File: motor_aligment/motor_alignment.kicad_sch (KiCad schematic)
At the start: 27 parts, among them J1 PWR_24V_IN, J2 SENSOR_IN, J3 LCD_I2C, J4 UART_DOWNLOAD, J5 JTAG, SW1 BTN, U1 LM2596S-5, U2 ADS1115, U3 ESP32-WROOM-32

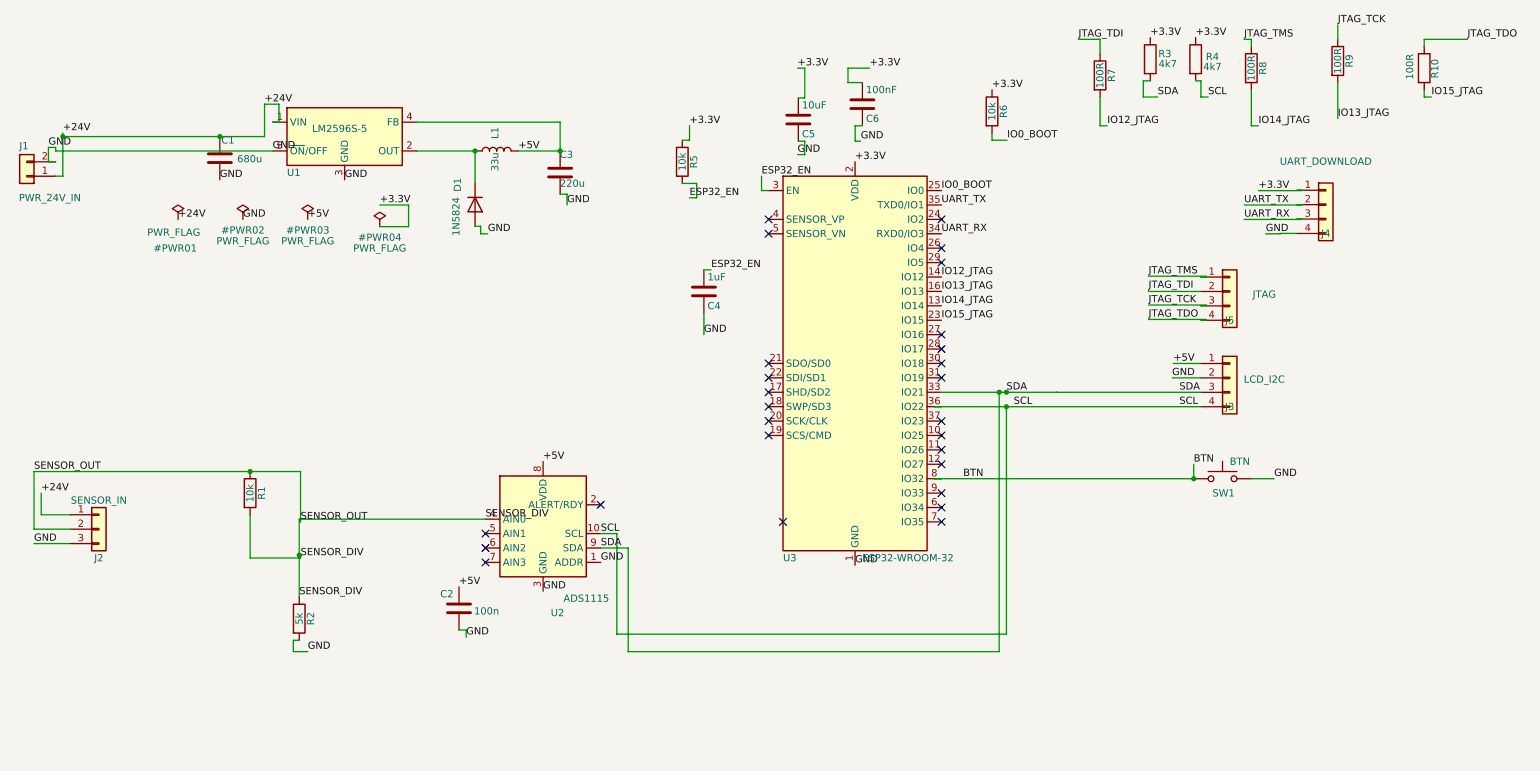
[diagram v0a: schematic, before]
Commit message: Add LCSC parameters and fix footprints for all components
- Added MPN, Manufacturer, JLCPCB_Type, Description, Datasheet properties
  to all 22 components from LCSC/JLCPCB database
- Fixed footprint mismatch: R7-R10 and C2/C6 corrected from 0402 to 0603
  to match purchased LCSC components
- ERC: 0 errors, 0 warnings

Co-Authored-By: Claude Sonnet 4.6 <noreply@anthropic.com>
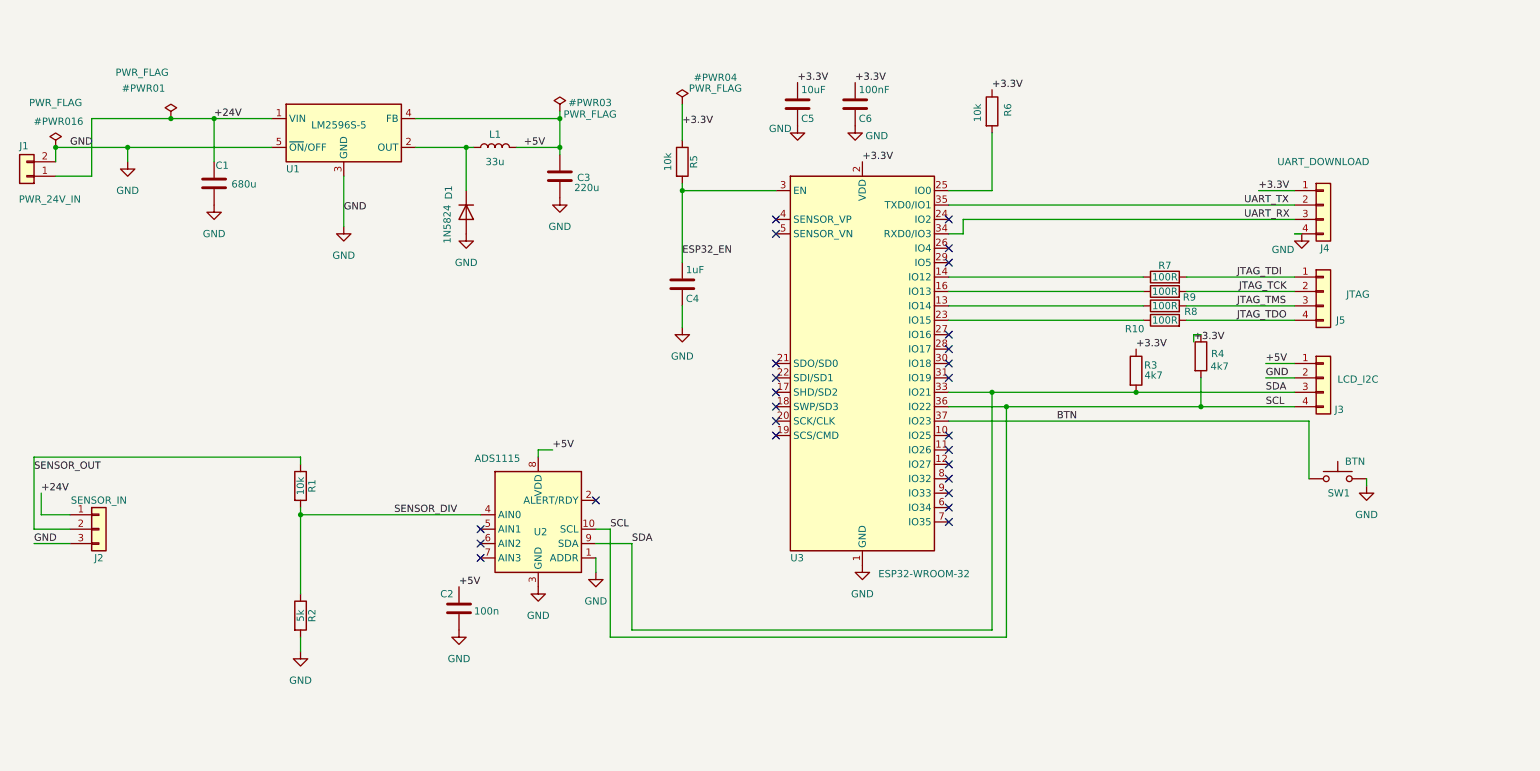
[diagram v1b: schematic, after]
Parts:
- C1: JLCPCB_Type (none) -> Extended; LCSC (none) -> C98216; MPN (none) -> RVT1V681M1213; Manufacturer (none) -> ROQANG
- C2, C6: footprint Capacitor_SMD:C_0402_1005Metric -> Capacitor_SMD:C_0603_1608Metric; JLCPCB_Type (none) -> Basic; LCSC (none) -> C14663; MPN (none) -> CC0603KRX7R9BB104; Manufacturer (none) -> YAGEO
- C3: JLCPCB_Type (none) -> Extended; LCSC (none) -> C3340; MPN (none) -> RVT1V221M0810; Manufacturer (none) -> Honor Elec
- C4: JLCPCB_Type (none) -> Basic; LCSC (none) -> C15849; MPN (none) -> CL10A105KB8NNNC; Manufacturer (none) -> Samsung Electro-Mechanics
- C5: JLCPCB_Type (none) -> Basic; LCSC (none) -> C15850; MPN (none) -> CL21A106KAYNNNE; Manufacturer (none) -> Samsung Electro-Mechanics
- D1: JLCPCB_Type (none) -> Basic; LCSC (none) -> C22452; MPN (none) -> SS54; Manufacturer (none) -> MDD（Microdiode Electronics）
- L1: JLCPCB_Type (none) -> Extended; LCSC (none) -> C840528; MPN (none) -> SRR1260-330M; Manufacturer (none) -> BOURNS
- R1, R5, R6: JLCPCB_Type (none) -> Basic; LCSC (none) -> C25804; MPN (none) -> 0603WAF1002T5E; Manufacturer (none) -> UNI-ROYAL(Uniroyal Elec)
- R10, R7, R8, R9: footprint Resistor_SMD:R_0402_1005Metric -> Resistor_SMD:R_0603_1608Metric; JLCPCB_Type (none) -> Basic; LCSC (none) -> C22775; MPN (none) -> 0603WAF1000T5E; Manufacturer (none) -> UNI-ROYAL(Uniroyal Elec)
- R2: JLCPCB_Type (none) -> Basic; LCSC (none) -> C23186; MPN (none) -> 0603WAF5101T5E; Manufacturer (none) -> UNI-ROYAL(Uniroyal Elec)
- R3, R4: JLCPCB_Type (none) -> Basic; LCSC (none) -> C23162; MPN (none) -> 0603WAF4701T5E; Manufacturer (none) -> UNI-ROYAL(Uniroyal Elec)
- SW1: JLCPCB_Type (none) -> Extended; LCSC (none) -> C83919; MPN (none) -> K2-1103DP-J4CW-04; Manufacturer (none) -> Korean Hroparts Elec
- U1: JLCPCB_Type (none) -> Preferred; LCSC (none) -> C10002; MPN (none) -> LM2596SX-5.0/NOPB; Manufacturer (none) -> Texas Instruments
- U2: JLCPCB_Type (none) -> Extended; LCSC (none) -> C34842333; MPN (none) -> ADS1115LIDGSR; Manufacturer (none) -> Texas Instruments
- U3: JLCPCB_Type (none) -> Extended; LCSC (none) -> C82899; MPN (none) -> ESP32-WROOM-32-N4; Manufacturer (none) -> Espressif Systems
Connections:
- net BTN: now also U3.37 (IO23); no longer U3.8 (IO32)
- net JTAG_TCK: now also J5.2 (Pin_2), R9.2; no longer J5.3 (Pin_3), R9.1
- net JTAG_TDI: now also J5.1 (Pin_1), R7.2; no longer J5.2 (Pin_2), R7.1
- net JTAG_TDO: now also R10.2; no longer R10.1
- net JTAG_TMS: now also J5.3 (Pin_3), R8.2; no longer J5.1 (Pin_1), R8.1
- net IO0_BOOT: no longer names the net of R6.2, U3.25 (IO0)
- net IO12_JTAG: no longer names the net of U3.14 (IO12)
- net IO12_JTAG: now also R7.1; no longer R7.2
- net IO13_JTAG: no longer names the net of U3.16 (IO13)
- net IO13_JTAG: now also R9.1; no longer R9.2
- net IO14_JTAG: no longer names the net of U3.13 (IO14)
- net IO14_JTAG: now also R8.1; no longer R8.2
- net IO15_JTAG: no longer names the net of U3.23 (IO15)
- net IO15_JTAG: now also R10.1; no longer R10.2
- no-connect marks 27 -> 26
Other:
- moved on the sheet: C1, C3, C4, C5, C6, D1, J3, J5, L1, R1, R10, R2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

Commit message: Clean PCB layout: remove all traces/vias, fix component placement
- Remove all routing segments and vias (to be re-routed manually)
- Fix LCSC/MPN/Manufacturer/JLCPCB_Type properties on all 22 components
- Fix R7-R10 and C2/C6 footprints from 0402 to 0603
- Assign PinHeader_1x04 footprint to J4/J5
- Place components per LM2596 datasheet layout (pp. 31-32)
- Resolve courtyard overlaps and ESP32 antenna keepout violations
- DRC: 0 errors, 1 warning (lib_footprint_mismatch)

Co-Authored-By: Claude Sonnet 4.6 <noreply@anthropic.com>
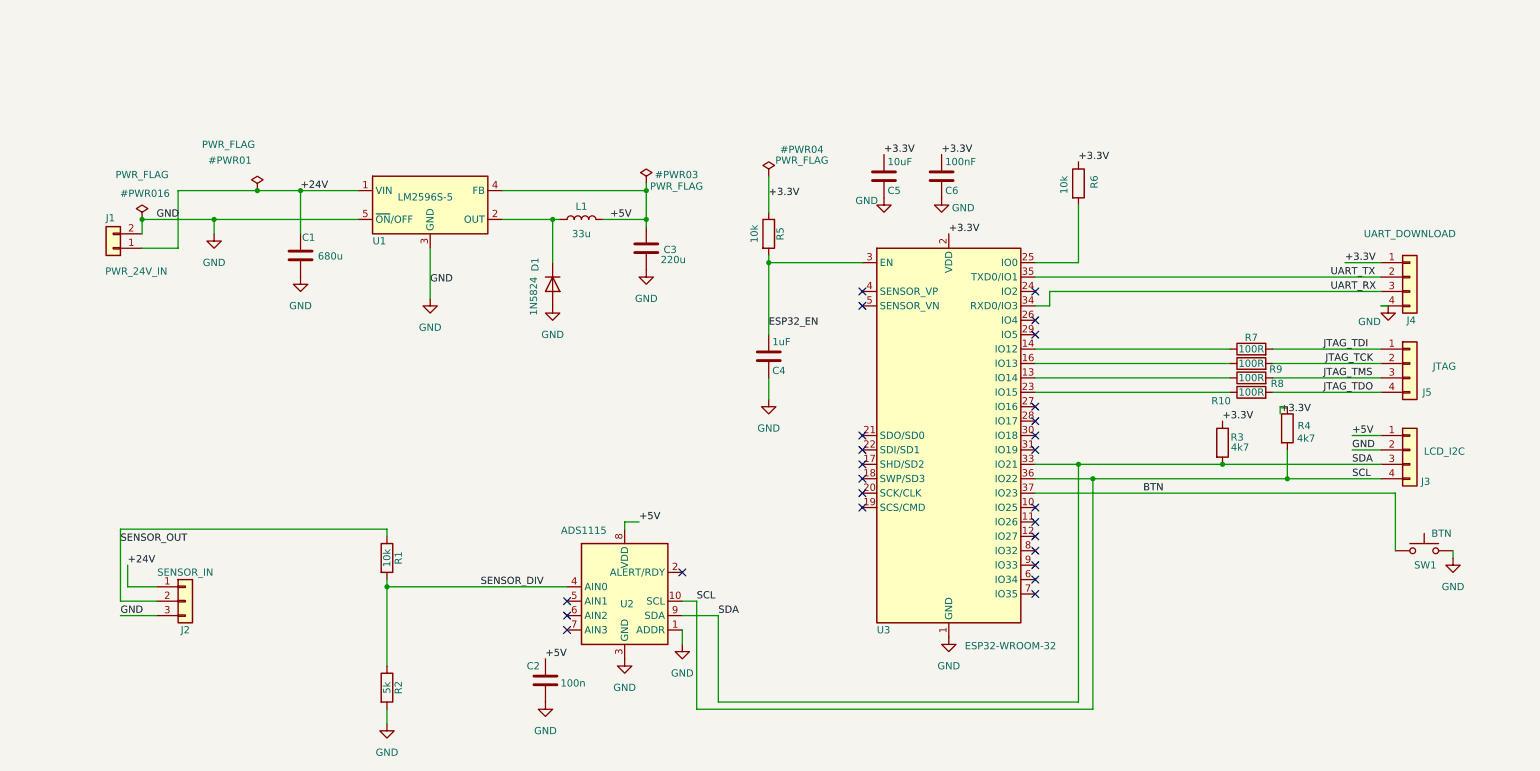
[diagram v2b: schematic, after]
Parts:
- J4, J5: footprint (none) -> Connector_PinHeader_2.54mm:PinHeader_1x04_P2.54mm_Vertical
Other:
- moved on the sheet: C1, C2, C3, C4, C5, C6, D1, J1, J2, J3, J4, J5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
